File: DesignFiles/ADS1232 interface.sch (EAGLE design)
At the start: 29 parts

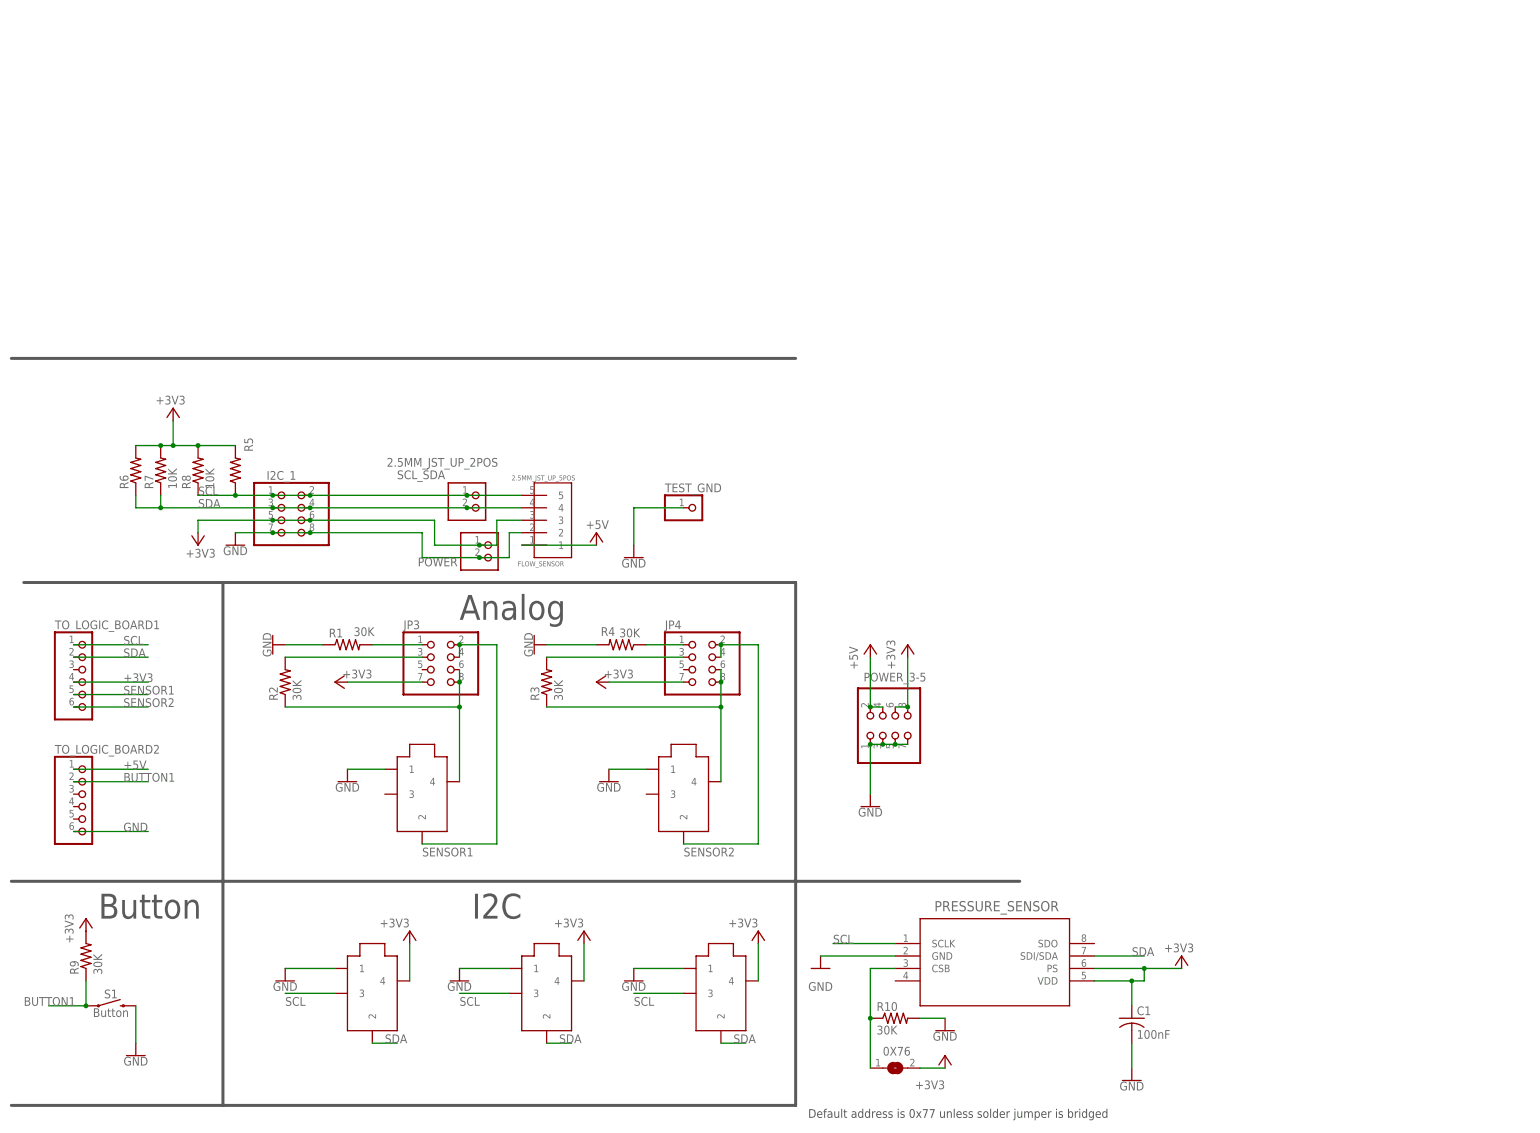
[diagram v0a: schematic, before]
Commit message: Additional PCBs
Added ADS1232 and pressure sensor PCBs. Removed sensor pcb
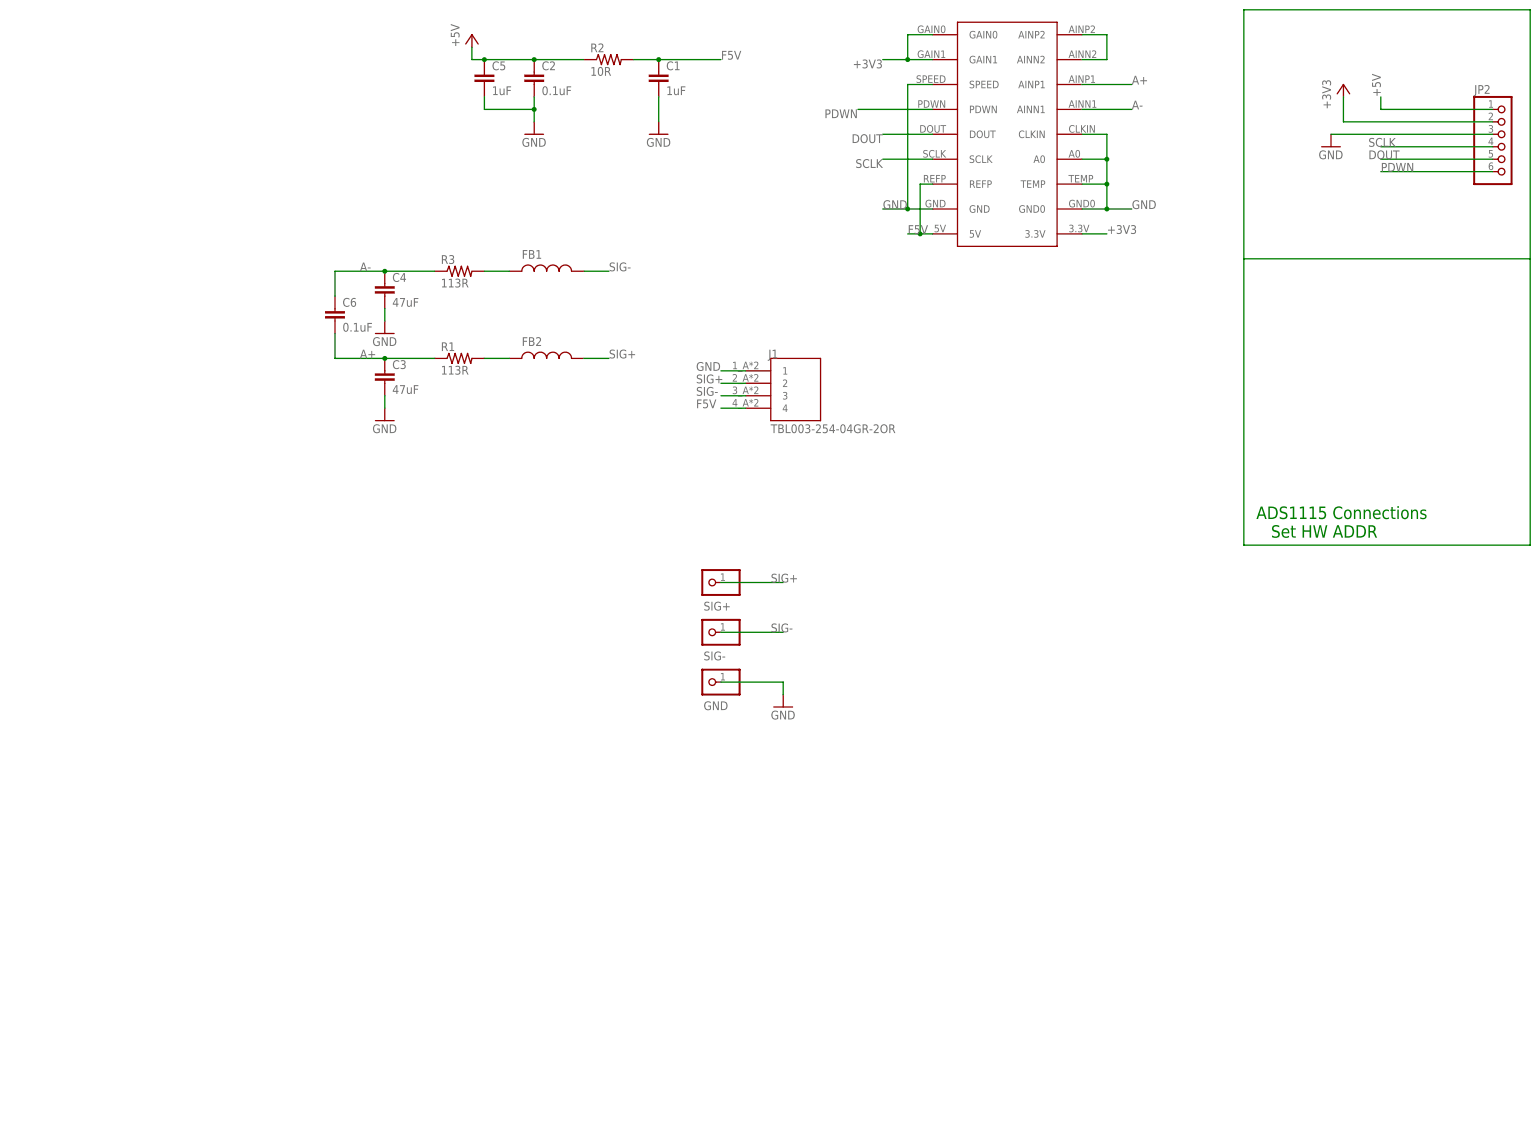
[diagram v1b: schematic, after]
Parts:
- removed 0X76: (no value), jumper:SJ
- removed ANALOG1, ANALOG2: AUDIOJACK_2.5MM_SMD, myHeaders:AUDIOJACK_2.5MM_SMD
- removed FLOW_SENSOR: 2.5MM_JST_UP_5POS, eDNA:2.5MM_JST_UP_5POS
- removed I2C_1, JP3, JP4, POWER_3-5: (no value), adafruit:PINHD-2X4
- removed POWER, SCL_SDA: 2.5MM_JST_UP_2POS, eDNA:2.5MM_JST_UP_2POS
- removed PRESSURE_SENSOR: MS580302BA01-00, eDNA:MS580302BA01-00
- removed R10, R4, R9: 30K, adafruit:R-US_R1206
- removed R5, R6: (no value), adafruit:R-US_R1206
- removed R7, R8: 10K, adafruit:R-US_0204/7
- removed S1: Button, SparkFun-Switches:MOMENTARY-SWITCH-SPST-PTH-6.0MM
- removed TEST_GND: (no value), adafruit:PINHD-1X1
- removed TO_LOGIC_BOARD1, TO_LOGIC_BOARD2: (no value), adafruit:PINHD-1X6CB
- removed U$1, U$2, U$5: I2C, myHeaders:AUDIOJACK_2.5MM_SMD
- added ADS1232: ADS1232, my_lib:ADS1232
- added C2, C6: 0.1uF, rcl:C-EUC0805
- added C3, C4: 47uF, rcl:C-EUC0805
- added C5: 1uF, rcl:C-EUC0805
- added FB1, FB2: (no value), Wurth_Elektronik_Passive_rev19e:WE-RFI_0805A_744760282A
- added GND, SIG+, SIG-: (no value), pinhead:PINHD-1X1
- added J1: TBL003-254-04GR-2OR, TBL003-254-04GR-2OR:TBL003-254-04GR-2OR
- added JP2: (no value), adafruit:PINHD-1X6
- C1: value 100nF -> 1uF; device adafruit:C-USC1206 -> rcl:C-EUC0805
- R1, R3: value 30K -> 113R; device adafruit:R-US_R1206 -> rcl:R-US_R0805
- R2: value 30K -> 10R; device adafruit:R-US_R1206 -> rcl:R-US_R0805
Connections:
- removed net BUTTON1: R9.1, S1.1, TO_LOGIC_BOARD2.2
- removed net N$1: 0X76.1, PRESSURE_SENSOR.CSB, R10.1
- removed net N$3: ANALOG1.4, JP3.6, JP3.8, R2.1
- removed net N$6: JP4.3, R3.2
- removed net N$7: ANALOG2.4, JP4.6, JP4.8, R3.1
- removed net N$8: JP4.1, R4.1
- removed net SCL: FLOW_SENSOR.5, I2C_1.1, I2C_1.2, PRESSURE_SENSOR.SCLK, R5.1, R8.1, SCL_SDA.1, TO_LOGIC_BOARD1.1, U$1.3, U$2.3, U$5.3
- removed net SDA: FLOW_SENSOR.4, I2C_1.3, I2C_1.4, PRESSURE_SENSOR.SDI/SDA, R6.1, R7.1, SCL_SDA.2, TO_LOGIC_BOARD1.2, U$1.2, U$2.2, U$5.2
- removed net SENSOR1: ANALOG1.2, JP3.2, JP3.4, TO_LOGIC_BOARD1.5
- removed net SENSOR2: ANALOG2.2, JP4.2, JP4.4, TO_LOGIC_BOARD1.6
- new net A+: ADS1232.AINP1, C3.1, C6.2, R1.1
- new net A-: ADS1232.AINN1, C4.1, C6.1, R3.1
- new net DOUT: ADS1232.DOUT, JP2.5
- new net F5V: ADS1232.5V, ADS1232.REFP, C1.1, J1.4, R2.2
- new net PDWN: ADS1232.PDWN, JP2.6
- new net SCLK: ADS1232.SCLK, JP2.4
- new net SIG+: FB2.2, J1.2, SIG+.1
- new net SIG-: FB1.2, J1.3, SIG-.1
- net +3V3: now also ADS1232.3.3V, ADS1232.GAIN0, ADS1232.GAIN1, JP2.2; no longer 0X76.2, C1.1, FLOW_SENSOR.3, I2C_1.5, I2C_1.6, JP3.7, JP4.7, POWER.1, POWER_3-5.6, POWER_3-5.8, PRESSURE_SENSOR.PS, PRESSURE_SENSOR.VDD, R5.2, R6.2, R7.2, R8.2, R9.2, TO_LOGIC_BOARD1.4, U$1.4, U$2.4, U$5.4
- net +5V: now also C2.1, C5.1, JP2.1, R2.1; no longer FLOW_SENSOR.1, POWER_3-5.2, POWER_3-5.4, TO_LOGIC_BOARD2.1
- net GND: now also ADS1232.A0, ADS1232.AINN2, ADS1232.AINP2, ADS1232.CLKIN, ADS1232.GND, ADS1232.GND0, ADS1232.SPEED, ADS1232.TEMP, C2.2, C3.2, C4.2, C5.2, GND.1, J1.1, JP2.3; no longer ANALOG1.1, ANALOG2.1, FLOW_SENSOR.2, I2C_1.7, I2C_1.8, POWER.2, POWER_3-5.1, POWER_3-5.3, POWER_3-5.5, POWER_3-5.7, PRESSURE_SENSOR.GND, R1.1, R10.2, R4.2, S1.2, TEST_GND.1, TO_LOGIC_BOARD2.6, U$1.1, U$2.1, U$5.1
- net N$4: now also FB1.1, R3.2; no longer JP3.3, R2.2
- net N$5: now also FB2.1; no longer JP3.1
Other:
- note added: "ADS1115 Connections Set HW ADDR"
- note removed: "Analog"
- note removed: "Button"
- note removed: "Default address is 0x77 unless solder jumper is bridged"
- note removed: "I2C"
- moved on the sheet: C1, R1, R2, R3
